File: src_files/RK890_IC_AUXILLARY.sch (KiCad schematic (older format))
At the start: 16 parts

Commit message: littleupdate
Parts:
- C58, C59, C60, C61, C62, C63, C64: renamed from C?; footprint (none) -> Capacitor_SMD:C_0402_1005Metric
- R10, R11, R12, R13, R14, R8, R9: renamed from R?; footprint (none) -> Resistor_SMD:R_0402_1005Metric
- Y1: renamed from Y?; footprint (none) -> Crystal:Crystal_SMD_Qantek_QC5CB-2Pin_5x3.2mm
- gave numbers to parts that had none: 1
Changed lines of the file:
@@
 $Descr A4 11693 8268
 encoding utf-8
-Sheet 4 11
+Sheet 11 11
 Title ""
 Date ""
@@
 $EndDescr
 $Comp
-L Device:C_Small C?
+L Device:C_Small C61
 U 1 1 6218F06E
 P 4250 2250
-F 0 "C?" V 4200 2100 50  0000 L CNN
+F 0 "C61" V 4200 2100 50  0000 L CNN
 F 1 "1uF" V 4200 2325 50  0000 L CNN
-F 2 "" H 4250 2250 50  0001 C CNN
+F 2 "Capacitor_SMD:C_0402_1005Metric" H 4250 2250 50  0001 C CNN
 F 3 "~" H 4250 2250 50  0001 C CNN
 	1    4250 2250
@@
 $EndComp
 $Comp
-L OLIMEX_Power:GND #PWR?
+L OLIMEX_Power:GND #PWR0158
 U 1 1 6218F5D6
 P 4025 2250
-F 0 "#PWR?" H 4025 2000 50  0001 C CNN
+F 0 "#PWR0158" H 4025 2000 50  0001 C CNN
 F 1 "GND" H 4030 2077 50  0000 C CNN
 F 2 "" H 4025 2250 60  0000 C CNN
@@
 	4025 2250 4150 2250
 $Comp
-L OLIMEX_Power:GND #PWR?
+L OLIMEX_Power:GND #PWR0159
 U 1 1 62191FEB
 P 5650 5375
-F 0 "#PWR?" H 5650 5125 50  0001 C CNN
+F 0 "#PWR0159" H 5650 5125 50  0001 C CNN
 F 1 "GND" H 5655 5202 50  0000 C CNN
 F 2 "" H 5650 5375 60  0000 C CNN
@@
 	4225 2900 4225 2700
 $Comp
-L Device:C_Small C?
+L Device:C_Small C58
 U 1 1 62196A1B
 P 3300 2500
-F 0 "C?" V 3250 2350 50  0000 L CNN
+F 0 "C58" V 3250 2350 50  0000 L CNN
 F 1 "1uF" V 3250 2575 50  0000 L CNN
-F 2 "" H 3300 2500 50  0001 C CNN
+F 2 "Capacitor_SMD:C_0402_1005Metric" H 3300 2500 50  0001 C CNN
 F 3 "~" H 3300 2500 50  0001 C CNN
 	1    3300 2500
@@
 $EndComp
 $Comp
-L Device:C_Small C?
+L Device:C_Small C59
 U 1 1 62196ED9
 P 3300 2900
-F 0 "C?" V 3250 2750 50  0000 L CNN
+F 0 "C59" V 3250 2750 50  0000 L CNN
 F 1 "1uF" V 3250 2975 50  0000 L CNN
-F 2 "" H 3300 2900 50  0001 C CNN
+F 2 "Capacitor_SMD:C_0402_1005Metric" H 3300 2900 50  0001 C CNN
 F 3 "~" H 3300 2900 50  0001 C CNN
 	1    3300 2900
@@
 $EndComp
 $Comp
-L OLIMEX_Power:GND #PWR?
+L OLIMEX_Power:GND #PWR0160
 U 1 1 62197D3A
 P 2975 2725
-F 0 "#PWR?" H 2975 2475 50  0001 C CNN
+F 0 "#PWR0160" H 2975 2475 50  0001 C CNN
 F 1 "GND" H 2980 2552 50  0000 C CNN
 F 2 "" H 2975 2725 60  0000 C CNN
@@
 Connection ~ 3650 2900
 $Comp
-L Device:Crystal Y?
+L Device:Crystal Y1
 U 1 1 62195BE8
 P 3650 2750
-F 0 "Y?" V 3604 2881 50  0000 L CNN
+F 0 "Y1" V 3604 2881 50  0000 L CNN
 F 1 "32.768KHz" V 3695 2881 50  0000 L CNN
-F 2 "" H 3650 2750 50  0001 C CNN
+F 2 "Crystal:Crystal_SMD_Qantek_QC5CB-2Pin_5x3.2mm" H 3650 2750 50  0001 C CNN
 F 3 "~" H 3650 2750 50  0001 C CNN
 	1    3650 2750
@@
 $Comp
 L GCL_Integrated-Circuits:RK809 U?
-U 1 1 6218E13D
+U 2 1 6218E13D
 P 5675 1950
 AR Path="/6218E13D" Ref="U?"  Part="1"
-AR Path="/62188C68/6218E13D" Ref="U?"  Part="1"
-F 0 "U?" H 5325 2125 50  0000 C CNN
+AR Path="/62188C68/6218E13D" Ref="U2"  Part="2"
+F 0 "U2" H 5325 2125 50  0000 C CNN
 F 1 "RK809" H 5325 2025 50  0000 C CNN
 F 2 "" H 5575 2150 50  0001 C CNN
 F 3 "" H 5575 2150 50  0001 C CNN
-	1    5675 1950
+	2    5675 1950
 	1    0    0    -1
 $EndComp
@@
 	3825 4100 4325 4100
 $Comp
-L Device:R_US R?
+L Device:R_US R10
 U 1 1 621A08B9
 P 3675 4100
-F 0 "R?" V 3470 4100 50  0000 C CNN
+F 0 "R10" V 3470 4100 50  0000 C CNN
 F 1 "22R" V 3561 4100 50  0000 C CNN
-F 2 "" V 3715 4090 50  0001 C CNN
+F 2 "Resistor_SMD:R_0402_1005Metric" V 3715 4090 50  0001 C CNN
 F 3 "~" H 3675 4100 50  0001 C CNN
 	1    3675 4100
@@
 $EndComp
 $Comp
-L Device:R_US R?
+L Device:R_US R8
 U 1 1 621A1545
 P 3025 3850
-F 0 "R?" H 3093 3896 50  0000 L CNN
+F 0 "R8" H 3093 3896 50  0000 L CNN
 F 1 "10K" H 3093 3805 50  0000 L CNN
-F 2 "" V 3065 3840 50  0001 C CNN
+F 2 "Resistor_SMD:R_0402_1005Metric" V 3065 3840 50  0001 C CNN
 F 3 "~" H 3025 3850 50  0001 C CNN
 	1    3025 3850
@@
 GOES TO WIFI/BT\nMODULE
 $Comp
-L Device:C_Small C?
+L Device:C_Small C60
 U 1 1 621A4193
 P 3550 4425
-F 0 "C?" V 3600 4475 50  0000 L CNN
+F 0 "C60" V 3600 4475 50  0000 L CNN
 F 1 "100n" V 3600 4175 50  0000 L CNN
-F 2 "" H 3550 4425 50  0001 C CNN
+F 2 "Capacitor_SMD:C_0402_1005Metric" H 3550 4425 50  0001 C CNN
 F 3 "~" H 3550 4425 50  0001 C CNN
 	1    3550 4425
@@
 $EndComp
 $Comp
-L Device:R_US R?
+L Device:R_US R9
 U 1 1 621A570E
 P 3550 4675
-F 0 "R?" V 3625 4650 50  0000 L CNN
+F 0 "R9" V 3625 4650 50  0000 L CNN
 F 1 "10K" V 3475 4625 50  0000 L CNN
-F 2 "" V 3590 4665 50  0001 C CNN
+F 2 "Resistor_SMD:R_0402_1005Metric" V 3590 4665 50  0001 C CNN
 F 3 "~" H 3550 4675 50  0001 C CNN
 	1    3550 4675
@@
 $EndComp
 $Comp
-L Device:R_US R?
+L Device:R_US R11
 U 1 1 621A6EC0
 P 4025 4850
-F 0 "R?" V 4100 4825 50  0000 L CNN
+F 0 "R11" V 4100 4825 50  0000 L CNN
 F 1 "22R" V 3950 4800 50  0000 L CNN
-F 2 "" V 4065 4840 50  0001 C CNN
+F 2 "Resistor_SMD:R_0402_1005Metric" V 4065 4840 50  0001 C CNN
 F 3 "~" H 4025 4850 50  0001 C CNN
 	1    4025 4850
@@
 	4025 4425 4025 4675
 $Comp
-L OLIMEX_Power:GND #PWR?
+L OLIMEX_Power:GND #PWR0161
 U 1 1 621A89E4
 P 3075 4425
-F 0 "#PWR?" H 3075 4175 50  0001 C CNN
+F 0 "#PWR0161" H 3075 4175 50  0001 C CNN
 F 1 "GND" H 3080 4252 50  0000 C CNN
 F 2 "" H 3075 4425 60  0000 C CNN
@@
 	6650 2800 6650 3050
 $Comp
-L OLIMEX_Power:GND #PWR?
+L OLIMEX_Power:GND #PWR0162
 U 1 1 621B6942
 P 6850 2850
-F 0 "#PWR?" H 6850 2600 50  0001 C CNN
+F 0 "#PWR0162" H 6850 2600 50  0001 C CNN
 F 1 "GND" H 6855 2677 50  0000 C CNN
 F 2 "" H 6850 2850 60  0000 C CNN
@@
 PMIC_EXT_EN
 $Comp
-L Device:R_US R?
+L Device:R_US R12
 U 1 1 621BA307
 P 7250 3450
-F 0 "R?" V 7325 3425 50  0000 L CNN
+F 0 "R12" V 7325 3425 50  0000 L CNN
 F 1 "22R" V 7175 3400 50  0000 L CNN
-F 2 "" V 7290 3440 50  0001 C CNN
+F 2 "Resistor_SMD:R_0402_1005Metric" V 7290 3440 50  0001 C CNN
 F 3 "~" H 7250 3450 50  0001 C CNN
 	1    7250 3450
@@
 $EndComp
 $Comp
-L OLIMEX_Power:GND #PWR?
+L OLIMEX_Power:GND #PWR0163
 U 1 1 621BCBAF
 P 7625 3450
-F 0 "#PWR?" H 7625 3200 50  0001 C CNN
+F 0 "#PWR0163" H 7625 3200 50  0001 C CNN
 F 1 "GND" H 7630 3277 50  0000 C CNN
 F 2 "" H 7625 3450 60  0000 C CNN
@@
 	7025 3250 7400 3250
 $Comp
-L Device:C_Small C?
+L Device:C_Small C64
 U 1 1 621C16B0
 P 7600 3925
-F 0 "C?" H 7425 3925 50  0000 L CNN
+F 0 "C64" H 7425 3925 50  0000 L CNN
 F 1 "100n" H 7350 4025 50  0000 L CNN
-F 2 "" H 7600 3925 50  0001 C CNN
+F 2 "Capacitor_SMD:C_0402_1005Metric" H 7600 3925 50  0001 C CNN
 F 3 "~" H 7600 3925 50  0001 C CNN
 	1    7600 3925
@@
 $EndComp
 $Comp
-L Device:C_Small C?
+L Device:C_Small C63
 U 1 1 621C2F72
 P 6975 4075
-F 0 "C?" H 6800 4075 50  0000 L CNN
+F 0 "C63" H 6800 4075 50  0000 L CNN
 F 1 "100n" H 6725 4175 50  0000 L CNN
-F 2 "" H 6975 4075 50  0001 C CNN
+F 2 "Capacitor_SMD:C_0402_1005Metric" H 6975 4075 50  0001 C CNN
 F 3 "~" H 6975 4075 50  0001 C CNN
 	1    6975 4075
@@
 	6975 4375 6975 4350
 $Comp
-L OLIMEX_Power:GND #PWR?
+L OLIMEX_Power:GND #PWR0164
 U 1 1 621C5F2B
 P 6975 4375
-F 0 "#PWR?" H 6975 4125 50  0001 C CNN
+F 0 "#PWR0164" H 6975 4125 50  0001 C CNN
 F 1 "GND" H 6980 4202 50  0000 C CNN
 F 2 "" H 6975 4375 60  0000 C CNN
@@
 	7600 3650 7600 3825
 $Comp
-L Device:R_US R?
+L Device:R_US R13
 U 1 1 621CB508
 P 8225 3500
-F 0 "R?" H 8293 3546 50  0000 L CNN
+F 0 "R13" H 8293 3546 50  0000 L CNN
 F 1 "10K" H 8293 3455 50  0000 L CNN
-F 2 "" V 8265 3490 50  0001 C CNN
+F 2 "Resistor_SMD:R_0402_1005Metric" V 8265 3490 50  0001 C CNN
 F 3 "~" H 8225 3500 50  0001 C CNN
 	1    8225 3500
@@
 $EndComp
 $Comp
-L Device:R_US R?
+L Device:R_US R14
 U 1 1 621CD187
 P 8225 3975
-F 0 "R?" H 8293 4021 50  0000 L CNN
+F 0 "R14" H 8293 4021 50  0000 L CNN
 F 1 "33K" H 8293 3930 50  0000 L CNN
-F 2 "" V 8265 3965 50  0001 C CNN
+F 2 "Resistor_SMD:R_0402_1005Metric" V 8265 3965 50  0001 C CNN
 F 3 "~" H 8225 3975 50  0001 C CNN
 	1    8225 3975
@@
 Connection ~ 8225 3650
 $Comp
-L power:+5V #PWR?
+L power:+5V #PWR0165
 U 1 1 621D0B2C
 P 8225 3300
-F 0 "#PWR?" H 8225 3150 50  0001 C CNN
+F 0 "#PWR0165" H 8225 3150 50  0001 C CNN
 F 1 "+5V" H 8240 3473 50  0000 C CNN
 F 2 "" H 8225 3300 50  0001 C CNN
@@
 	8225 3300 8225 3350
 $Comp
-L OLIMEX_Power:GND #PWR?
+L OLIMEX_Power:GND #PWR0166
 U 1 1 621D2AE3
 P 8225 4200
-F 0 "#PWR?" H 8225 3950 50  0001 C CNN
+F 0 "#PWR0166" H 8225 3950 50  0001 C CNN
 F 1 "GND" H 8230 4027 50  0000 C CNN
 F 2 "" H 8225 4200 60  0000 C CNN
@@
 	8225 4200 8225 4125
 $Comp
-L OLIMEX_Power:GND #PWR?
+L OLIMEX_Power:GND #PWR0167
 U 1 1 621D52B2
 P 7675 2300
-F 0 "#PWR?" H 7675 2050 50  0001 C CNN
+F 0 "#PWR0167" H 7675 2050 50  0001 C CNN
 F 1 "GND" H 7680 2127 50  0000 C CNN
 F 2 "" H 7675 2300 60  0000 C CNN
@@
 $EndComp
 $Comp
-L Device:C_Small C?
+L Device:C_Small C62
 U 1 1 621D6B1A
 P 6875 2300
-F 0 "C?" V 6800 2150 50  0000 L CNN
+F 0 "C62" V 6800 2150 50  0000 L CNN
 F 1 "1U" V 6800 2400 50  0000 L CNN
-F 2 "" H 6875 2300 50  0001 C CNN
+F 2 "Capacitor_SMD:C_0402_1005Metric" H 6875 2300 50  0001 C CNN
 F 3 "~" H 6875 2300 50  0001 C CNN
 	1    6875 2300
@@
 P 6700 2150
 AR Path="/61CF51BC/621DB130" Ref="#PWR?"  Part="1"
-AR Path="/62188C68/621DB130" Ref="#PWR?"  Part="1"
-F 0 "#PWR?" H 6700 2000 50  0001 C CNN
+AR Path="/62188C68/621DB130" Ref="#PWR0168"  Part="1"
+F 0 "#PWR0168" H 6700 2000 50  0001 C CNN
 F 1 "+3V3" H 6715 2323 50  0000 C CNN
 F 2 "" H 6700 2150 50  0001 C CNN

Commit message: all screens added_3 items left
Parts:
- removed U2: RK809, symbol GCL_Integrated-Circuits:RK809
- added U2: RK809, symbol GCL_Integrated-Circuits:RK809
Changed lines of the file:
@@
 $Descr A4 11693 8268
 encoding utf-8
-Sheet 11 11
+Sheet 9 12
 Title ""
 Date ""
@@
 Wire Wire Line
 	4025 2250 4150 2250
-$Comp
-L OLIMEX_Power:GND #PWR0159
-U 1 1 62191FEB
-P 5650 5375
-F 0 "#PWR0159" H 5650 5125 50  0001 C CNN
-F 1 "GND" H 5655 5202 50  0000 C CNN
-F 2 "" H 5650 5375 60  0000 C CNN
-F 3 "" H 5650 5375 60  0000 C CNN
-	1    5650 5375
-	1    0    0    -1
-$EndComp
-Wire Wire Line
-	5575 5375 5650 5375
-Connection ~ 5650 5375
-Wire Wire Line
-	5650 5375 5725 5375
 Wire Wire Line
 	4225 2900 4225 2700
@@
 PMIC_SLEEP_H
 Wire Wire Line
-	5575 5250 5575 5375
-Wire Wire Line
 	4675 3450 4200 3450
 Wire Wire Line
@@
 	4675 3900 4225 3900
 Wire Wire Line
-	5725 5250 5725 5375
-Wire Wire Line
 	4350 2250 4675 2250
 Wire Wire Line
@@
 Wire Wire Line
 	4675 3050 4175 3050
-$Comp
-L GCL_Integrated-Circuits:RK809 U?
-U 2 1 6218E13D
-P 5675 1950
-AR Path="/6218E13D" Ref="U?"  Part="1"
-AR Path="/62188C68/6218E13D" Ref="U2"  Part="2"
-F 0 "U2" H 5325 2125 50  0000 C CNN
-F 1 "RK809" H 5325 2025 50  0000 C CNN
-F 2 "" H 5575 2150 50  0001 C CNN
-F 3 "" H 5575 2150 50  0001 C CNN
-	2    5675 1950
-	1    0    0    -1
-$EndComp
 Text Label 4450 4300 0    33   ~ 0
 RESETn
@@
 Wire Wire Line
 	6700 2300 6775 2300
+Wire Wire Line
+	5650 5450 5725 5450
+Connection ~ 5650 5450
+Wire Wire Line
+	5575 5450 5650 5450
+$Comp
+L OLIMEX_Power:GND #PWR0159
+U 1 1 62191FEB
+P 5650 5450
+F 0 "#PWR0159" H 5650 5200 50  0001 C CNN
+F 1 "GND" H 5655 5277 50  0000 C CNN
+F 2 "" H 5650 5450 60  0000 C CNN
+F 3 "" H 5650 5450 60  0000 C CNN
+	1    5650 5450
+	1    0    0    -1
+$EndComp
+Wire Wire Line
+	5575 5250 5575 5450
+Wire Wire Line
+	5725 5250 5725 5450
+$Comp
+L GCL_Integrated-Circuits:RK809 U2
+U 1 1 6260FEEB
+P 5675 1950
+F 0 "U2" H 5580 2115 50  0000 C CNN
+F 1 "RK809" H 5580 2024 50  0000 C CNN
+F 2 "" H 5575 2150 50  0001 C CNN
+F 3 "" H 5575 2150 50  0001 C CNN
+	1    5675 1950
+	1    0    0    -1
+$EndComp
 $EndSCHEMATC

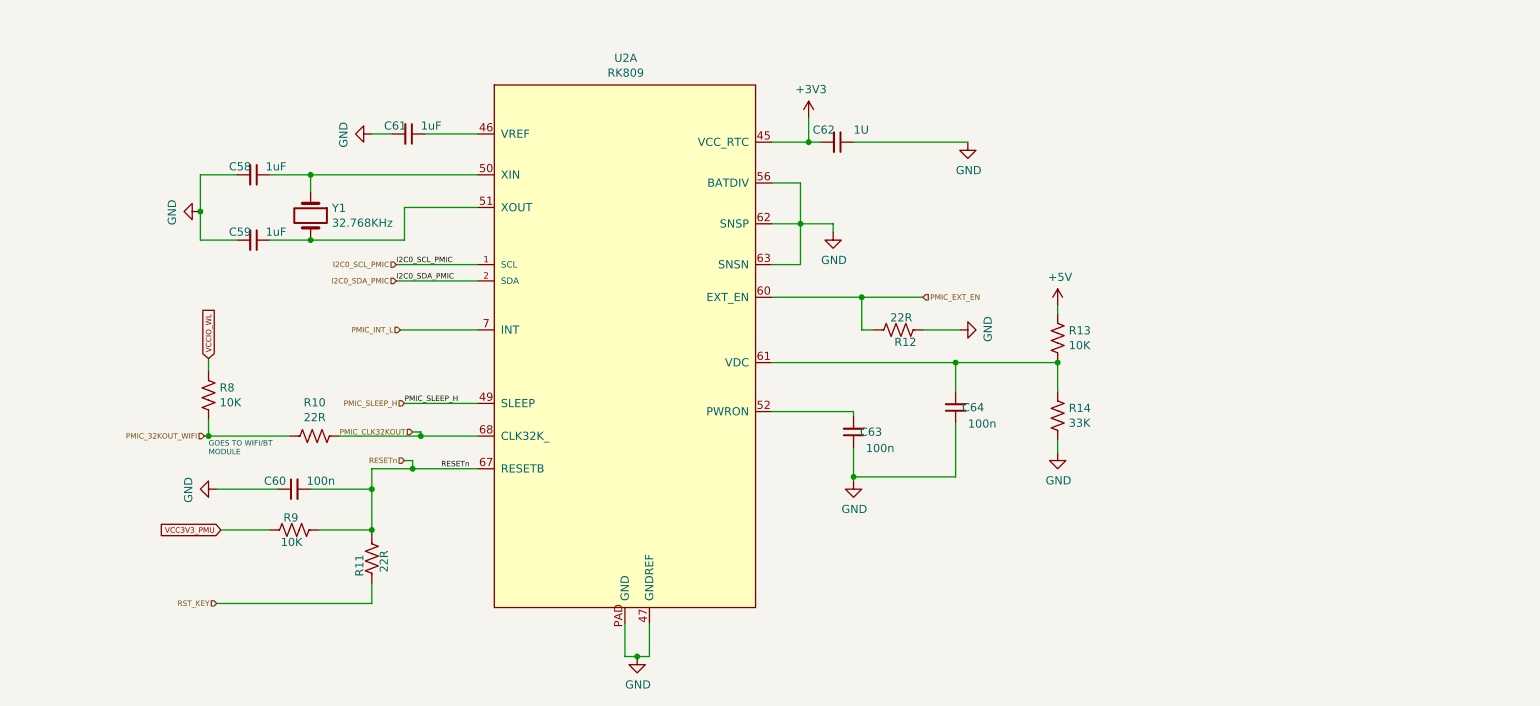
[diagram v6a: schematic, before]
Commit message: schematic capture complete
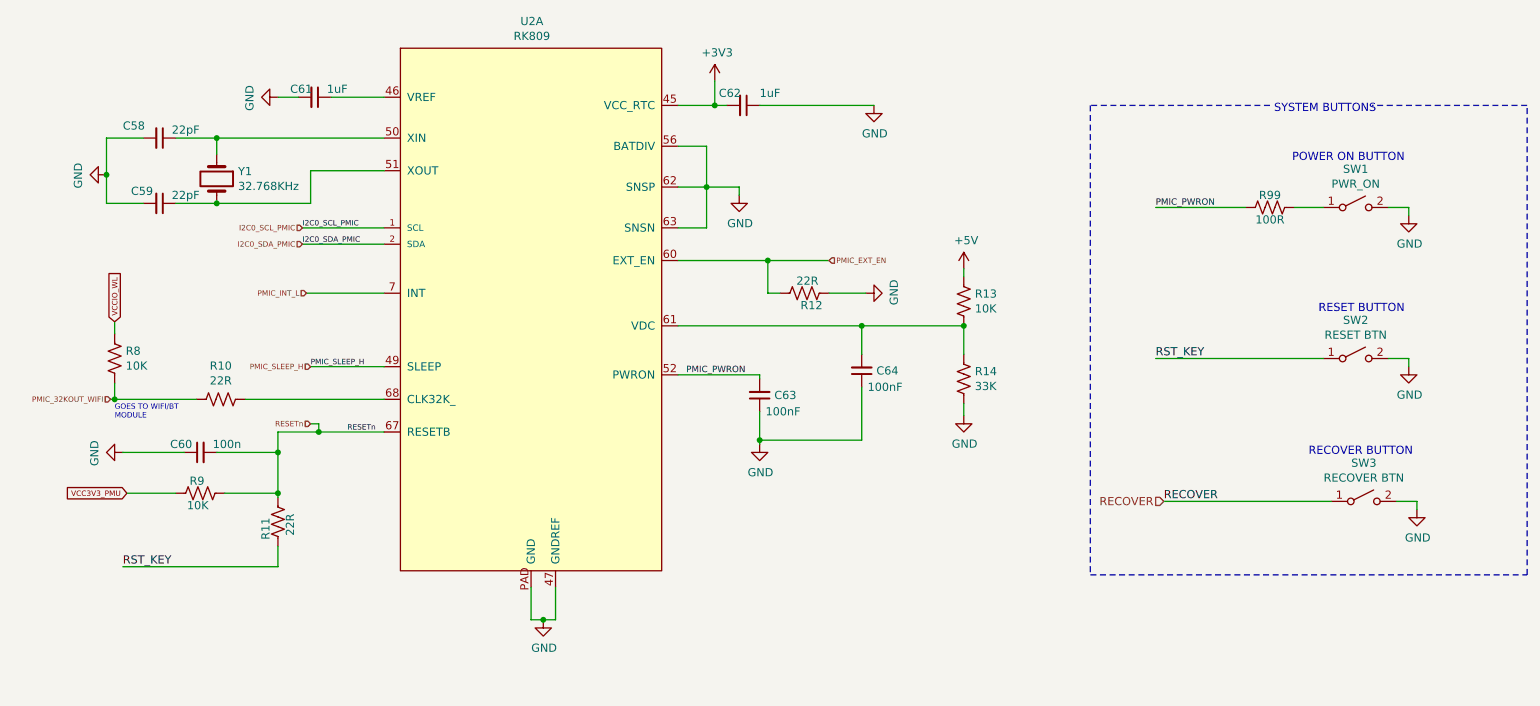
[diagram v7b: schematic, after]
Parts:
- added R99: 100R, Resistor_SMD:R_0402_1005Metric, symbol Device:R_US
- added SW1: PWR_ON, Button_Switch_SMD:SW_SPST_B3U-1000P-B, symbol Switch:SW_SPST
- added SW2: RESET BTN, Button_Switch_SMD:SW_SPST_B3U-1000P-B, symbol Switch:SW_SPST
- added SW3: RECOVER BTN, Button_Switch_SMD:SW_SPST_B3U-1000P-B, symbol Switch:SW_SPST
- C58, C59: value 1uF -> 22pF
- C62: value 1U -> 1uF
- C63, C64: value 100n -> 100nF
- R14: footprint Resistor_SMD:R_0402_1005Metric -> Resistor_SMD:R_0603_1608Metric
- U2: footprint (none) -> greencharge-footprints:QFN-68_EP_7x7_Pitch0.35mm
- Y1: footprint Crystal:Crystal_SMD_Qantek_QC5CB-2Pin_5x3.2mm -> Crystal:Crystal_SMD_MicroCrystal_CM9V-T1A-2Pin_1.6x1.0mm
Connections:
- net GND: now also SW1.2 (B), SW2.2 (B), SW3.2 (B)
- net RST_KEY: now also SW2.1 (A)
- net PMIC_PWRON: now reaches C63.2, U2.52 (PWRON)
- net PMIC_PWRON: now also R99.2
- net PMIC_CLK32KOUT: no longer names the net of R10.1, U2.68 (CLK32K_)
- new net: R99.1, SW1.1 (A)
- new net RECOVER: SW3.1 (A)
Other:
- note added: "POWER ON BUTTON\n"
- note added: "RECOVER BUTTON\n"
- note added: "RESET BUTTON\n"
- note added: "SYSTEM BUTTONS\n"
- moved on the sheet: C58, C59, C60, C61, C62, C63, C64, R10, R11, R12, R13, R14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
